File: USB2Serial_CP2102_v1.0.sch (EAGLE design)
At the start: 23 parts, among them CN1 UART, CN2 47346-0001, IC1 AMS1117-3.3, U3 CP2102

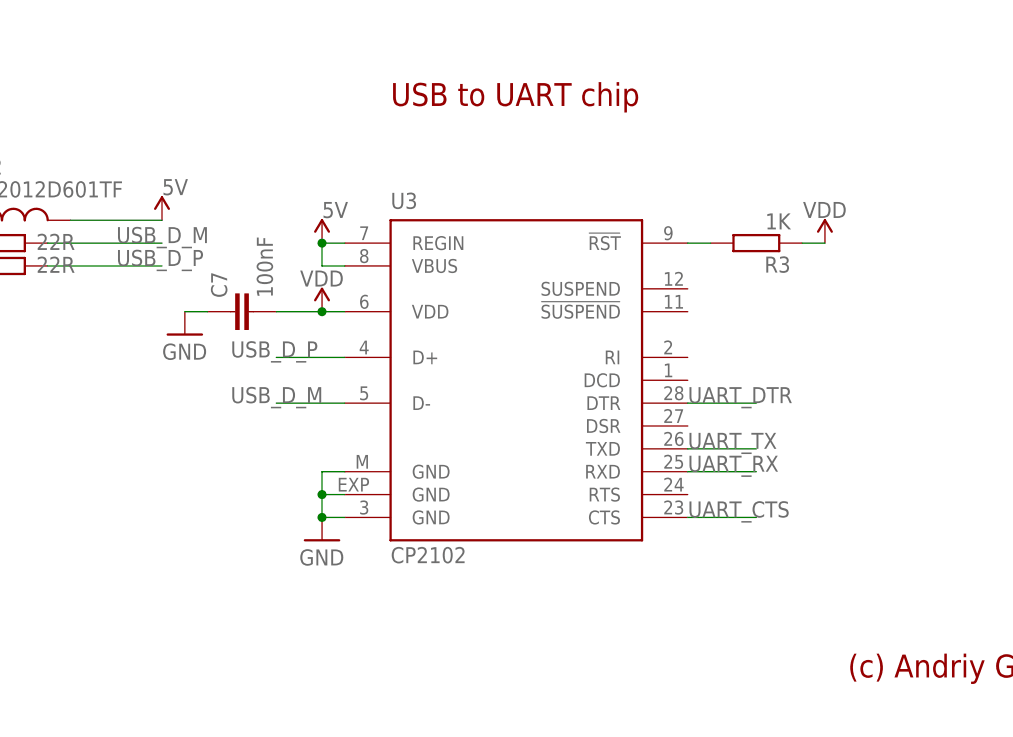
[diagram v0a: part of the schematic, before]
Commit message: Moved some traced around
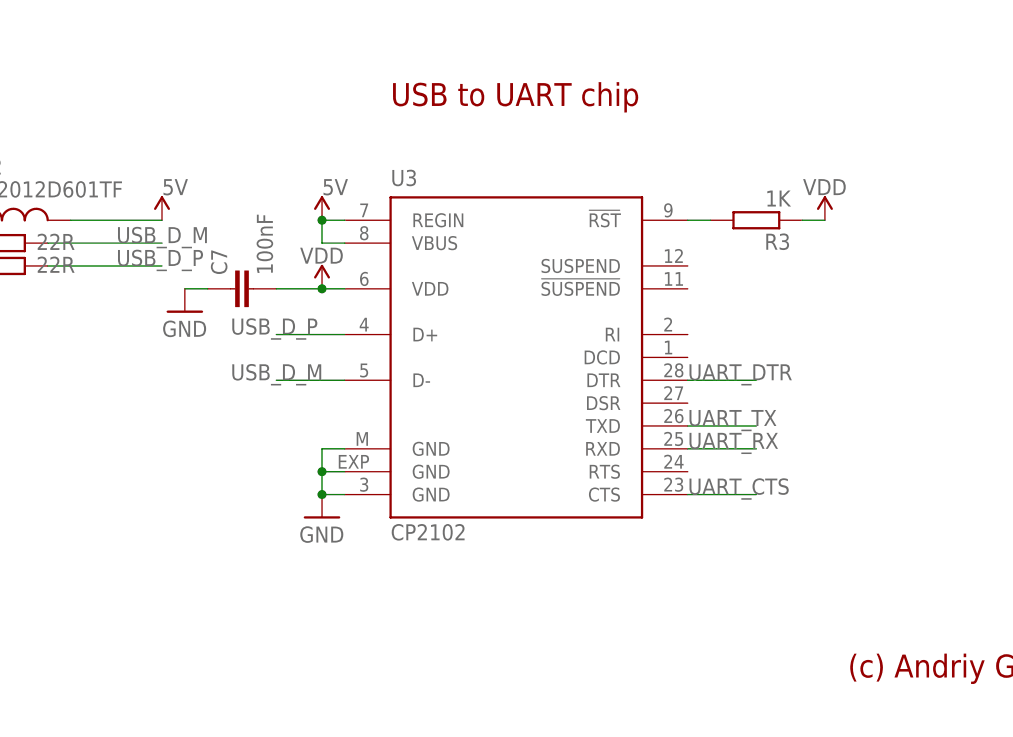
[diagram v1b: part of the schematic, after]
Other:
- moved on the sheet: C7, R3, U3
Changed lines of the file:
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@@
 <attribute name="VALUE" x="48.26" y="63.246" size="1.778" layer="96"/>
 </instance>
-<instance part="GND3" gate="1" x="106.68" y="43.18" smashed="yes">
-<attribute name="VALUE" x="104.14" y="40.386" size="1.778" layer="96"/>
-</instance>
-<instance part="C7" gate="G$1" x="96.52" y="68.58" smashed="yes" rot="R90">
-<attribute name="NAME" x="96.139" y="70.104" size="1.778" layer="95" rot="R90"/>
-<attribute name="VALUE" x="101.219" y="70.104" size="1.778" layer="96" rot="R90"/>
+<instance part="GND3" gate="1" x="106.68" y="45.72" smashed="yes">
+<attribute name="VALUE" x="104.14" y="42.926" size="1.778" layer="96"/>
+</instance>
+<instance part="C7" gate="G$1" x="96.52" y="71.12" smashed="yes" rot="R90">
+<attribute name="NAME" x="96.139" y="72.644" size="1.778" layer="95" rot="R90"/>
+<attribute name="VALUE" x="101.219" y="72.644" size="1.778" layer="96" rot="R90"/>
 </instance>
 <instance part="FRAME1" gate="G$1" x="0" y="0" smashed="yes"/>
@@
 <attribute name="VALUE" x="177.8" y="124.714" size="1.778" layer="96"/>
 </instance>
-<instance part="GND6" gate="1" x="91.44" y="66.04" smashed="yes">
-<attribute name="VALUE" x="88.9" y="63.246" size="1.778" layer="96"/>
+<instance part="GND6" gate="1" x="91.44" y="68.58" smashed="yes">
+<attribute name="VALUE" x="88.9" y="65.786" size="1.778" layer="96"/>
 </instance>
 <instance part="GND4" gate="1" x="119.38" y="111.76" smashed="yes">
@@
 <attribute name="VALUE" x="103.124" y="117.221" size="1.778" layer="96"/>
 </instance>
-<instance part="U3" gate="G$1" x="127" y="60.96" smashed="yes">
-<attribute name="NAME" x="114.3" y="80.01" size="1.778" layer="95"/>
-<attribute name="VALUE" x="114.3" y="40.64" size="1.778" layer="96"/>
-</instance>
-<instance part="SUPPLY4" gate="G$1" x="106.68" y="76.2" smashed="yes">
-<attribute name="VALUE" x="106.68" y="78.994" size="1.778" layer="96"/>
-</instance>
-<instance part="R3" gate="G$1" x="154.94" y="76.2" smashed="yes" rot="R180">
-<attribute name="NAME" x="158.75" y="74.7014" size="1.778" layer="95" rot="R180"/>
-<attribute name="VALUE" x="158.75" y="79.502" size="1.778" layer="96" rot="R180"/>
-</instance>
-<instance part="SUPPLY5" gate="VDD" x="162.56" y="76.2" smashed="yes">
-<attribute name="VALUE" x="162.56" y="78.994" size="1.778" layer="96" align="bottom-center"/>
-</instance>
-<instance part="SUPPLY6" gate="VDD" x="106.68" y="68.58" smashed="yes">
-<attribute name="VALUE" x="106.68" y="71.374" size="1.778" layer="96" align="bottom-center"/>
+<instance part="U3" gate="G$1" x="127" y="63.5" smashed="yes">
+<attribute name="NAME" x="114.3" y="82.55" size="1.778" layer="95"/>
+<attribute name="VALUE" x="114.3" y="43.18" size="1.778" layer="96"/>
+</instance>
+<instance part="SUPPLY4" gate="G$1" x="106.68" y="78.74" smashed="yes">
+<attribute name="VALUE" x="106.68" y="81.534" size="1.778" layer="96"/>
+</instance>
+<instance part="R3" gate="G$1" x="154.94" y="78.74" smashed="yes" rot="R180">
+<attribute name="NAME" x="158.75" y="77.2414" size="1.778" layer="95" rot="R180"/>
+<attribute name="VALUE" x="158.75" y="82.042" size="1.778" layer="96" rot="R180"/>
+</instance>
+<instance part="SUPPLY5" gate="VDD" x="162.56" y="78.74" smashed="yes">
+<attribute name="VALUE" x="162.56" y="81.534" size="1.778" layer="96" align="bottom-center"/>
+</instance>
+<instance part="SUPPLY6" gate="VDD" x="106.68" y="71.12" smashed="yes">
+<attribute name="VALUE" x="106.68" y="73.914" size="1.778" layer="96" align="bottom-center"/>
 </instance>
 </instances>
@@
 </segment>
 <segment>
-<wire x1="109.22" y1="45.72" x2="106.68" y2="45.72" width="0.1524" layer="91"/>
+<wire x1="109.22" y1="48.26" x2="106.68" y2="48.26" width="0.1524" layer="91"/>
 <pinref part="GND3" gate="1" pin="GND"/>
 <pinref part="U3" gate="G$1" pin="GND"/>
-<wire x1="106.68" y1="45.72" x2="106.68" y2="48.26" width="0.1524" layer="91"/>
-<junction x="106.68" y="45.72"/>
+<wire x1="106.68" y1="48.26" x2="106.68" y2="50.8" width="0.1524" layer="91"/>
+<junction x="106.68" y="48.26"/>
 <pinref part="U3" gate="G$1" pin="GND@M"/>
-<wire x1="106.68" y1="48.26" x2="106.68" y2="50.8" width="0.1524" layer="91"/>
-<wire x1="106.68" y1="50.8" x2="109.22" y2="50.8" width="0.1524" layer="91"/>
+<wire x1="106.68" y1="50.8" x2="106.68" y2="53.34" width="0.1524" layer="91"/>
+<wire x1="106.68" y1="53.34" x2="109.22" y2="53.34" width="0.1524" layer="91"/>
 <pinref part="U3" gate="G$1" pin="GND@EXP"/>
-<wire x1="109.22" y1="48.26" x2="106.68" y2="48.26" width="0.1524" layer="91"/>
-<junction x="106.68" y="48.26"/>
+<wire x1="109.22" y1="50.8" x2="106.68" y2="50.8" width="0.1524" layer="91"/>
+<junction x="106.68" y="50.8"/>
 </segment>
 <segment>
@@
 <segment>
 <pinref part="C7" gate="G$1" pin="1"/>
-<wire x1="93.98" y1="68.58" x2="91.44" y2="68.58" width="0.1524" layer="91"/>
+<wire x1="93.98" y1="71.12" x2="91.44" y2="71.12" width="0.1524" layer="91"/>
 <pinref part="GND6" gate="1" pin="GND"/>
 </segment>
@@
 </segment>
 <segment>
+<wire x1="109.22" y1="78.74" x2="106.68" y2="78.74" width="0.1524" layer="91"/>
 <wire x1="109.22" y1="76.2" x2="106.68" y2="76.2" width="0.1524" layer="91"/>
-<wire x1="109.22" y1="73.66" x2="106.68" y2="73.66" width="0.1524" layer="91"/>
-<wire x1="106.68" y1="73.66" x2="106.68" y2="76.2" width="0.1524" layer="91"/>
+<wire x1="106.68" y1="76.2" x2="106.68" y2="78.74" width="0.1524" layer="91"/>
 <pinref part="U3" gate="G$1" pin="REGIN"/>
 <pinref part="U3" gate="G$1" pin="VBUS"/>
 <pinref part="SUPPLY4" gate="G$1" pin="5V"/>
-<junction x="106.68" y="76.2"/>
+<junction x="106.68" y="78.74"/>
 </segment>
 </net>
@@
 </segment>
 <segment>
-<wire x1="109.22" y1="63.5" x2="101.6" y2="63.5" width="0.1524" layer="91"/>
-<label x="96.52" y="63.5" size="1.778" layer="95"/>
+<wire x1="109.22" y1="66.04" x2="101.6" y2="66.04" width="0.1524" layer="91"/>
+<label x="96.52" y="66.04" size="1.778" layer="95"/>
 <pinref part="U3" gate="G$1" pin="D+"/>
 </segment>
@@
 </segment>
 <segment>
-<wire x1="109.22" y1="58.42" x2="101.6" y2="58.42" width="0.1524" layer="91"/>
-<label x="96.52" y="58.42" size="1.778" layer="95"/>
+<wire x1="109.22" y1="60.96" x2="101.6" y2="60.96" width="0.1524" layer="91"/>
+<label x="96.52" y="60.96" size="1.778" layer="95"/>
 <pinref part="U3" gate="G$1" pin="D-"/>
 </segment>
@@
 </segment>
 <segment>
-<wire x1="147.32" y1="58.42" x2="154.94" y2="58.42" width="0.1524" layer="91"/>
-<label x="147.32" y="58.42" size="1.778" layer="95"/>
+<wire x1="147.32" y1="60.96" x2="154.94" y2="60.96" width="0.1524" layer="91"/>
+<label x="147.32" y="60.96" size="1.778" layer="95"/>
 <pinref part="U3" gate="G$1" pin="DTR"/>
 </segment>
@@
 </segment>
 <segment>
-<wire x1="147.32" y1="50.8" x2="154.94" y2="50.8" width="0.1524" layer="91"/>
-<label x="147.32" y="50.8" size="1.778" layer="95"/>
+<wire x1="147.32" y1="53.34" x2="154.94" y2="53.34" width="0.1524" layer="91"/>
+<label x="147.32" y="53.34" size="1.778" layer="95"/>
 <pinref part="U3" gate="G$1" pin="RXD"/>
 </segment>
@@
 </segment>
 <segment>
-<wire x1="147.32" y1="53.34" x2="154.94" y2="53.34" width="0.1524" layer="91"/>
-<label x="147.32" y="53.34" size="1.778" layer="95"/>
+<wire x1="147.32" y1="55.88" x2="154.94" y2="55.88" width="0.1524" layer="91"/>
+<label x="147.32" y="55.88" size="1.778" layer="95"/>
 <pinref part="U3" gate="G$1" pin="TXD"/>
 </segment>
@@
 </segment>
 <segment>
-<wire x1="147.32" y1="45.72" x2="154.94" y2="45.72" width="0.1524" layer="91"/>
-<label x="147.32" y="45.72" size="1.778" layer="95"/>
+<wire x1="147.32" y1="48.26" x2="154.94" y2="48.26" width="0.1524" layer="91"/>
+<label x="147.32" y="48.26" size="1.778" layer="95"/>
 <pinref part="U3" gate="G$1" pin="CTS"/>
 </segment>
@@
 <pinref part="U3" gate="G$1" pin="!RST"/>
 <pinref part="R3" gate="G$1" pin="2"/>
-<wire x1="147.32" y1="76.2" x2="149.86" y2="76.2" width="0.1524" layer="91"/>
+<wire x1="147.32" y1="78.74" x2="149.86" y2="78.74" width="0.1524" layer="91"/>
 </segment>
 </net>
@@
 <segment>
 <pinref part="R3" gate="G$1" pin="1"/>
-<wire x1="160.02" y1="76.2" x2="162.56" y2="76.2" width="0.1524" layer="91"/>
+<wire x1="160.02" y1="78.74" x2="162.56" y2="78.74" width="0.1524" layer="91"/>
 <pinref part="SUPPLY5" gate="VDD" pin="VDD"/>
 </segment>
@@
 <pinref part="U3" gate="G$1" pin="VDD"/>
 <pinref part="C7" gate="G$1" pin="2"/>
-<wire x1="109.22" y1="68.58" x2="106.68" y2="68.58" width="0.1524" layer="91"/>
+<wire x1="109.22" y1="71.12" x2="106.68" y2="71.12" width="0.1524" layer="91"/>
 <pinref part="SUPPLY6" gate="VDD" pin="VDD"/>
-<wire x1="106.68" y1="68.58" x2="101.6" y2="68.58" width="0.1524" layer="91"/>
-<junction x="106.68" y="68.58"/>
-</segment>
-</net>
+<wire x1="106.68" y1="71.12" x2="101.6" y2="71.12" width="0.1524" layer="91"/>
+<junction x="106.68" y="71.12"/>
+</segment>
+</net>
